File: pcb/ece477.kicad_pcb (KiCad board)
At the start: 2 copper layers, 44 x 40 mm, 16 parts, among them J1 USB_A, SW1 SW_DIP_x01, U1 ESP32-WROOM-32, U2 FT232RL-REEL, U3 LM3671, U4 ADA254, U5 ADA751

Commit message: squeezed lm3671 components together
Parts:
- moved L1 5.10 mm to (170.0, 86.0)
- moved C2 4.00 mm to (170.0, 84.0), turned to 270 degrees
- moved U3 4.00 mm to (173.0, 85.0)
- moved C3 0.34 mm to (174.3, 87.0), turned to 180 degrees
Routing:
- net Net-(C3-Pad2): track 21.0 -> 9.60 mm, vias 2 -> 0
- net Net-(C2-Pad2): track 99.5 -> 90.6 mm
- net Net-(L1-Pad2): track 3.29 -> 1.84 mm
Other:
- board text added: "1"

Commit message: pcb update
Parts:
- removed J1: USB_A, digikey-footprints:USB_Mini_B_Female_690-005-299-043
- removed U1: ESP32-WROOM-32, digikey-footprints:ESP32-WROOM-32D
- removed U4: ADA254, Connector_PinSocket_2.00mm:PinSocket_1x08_P2.00mm_Vertical
- added ADA 254: ADA254, Connector_PinSocket_2.00mm:PinSocket_1x08_P2.00mm_Vertical, F.Cu at (154.0, 111.0)
- added ESP32: ESP32-WROOM-32, digikey-footprints:ESP32-WROOM-32D, F.Cu at (159.0, 98.0)
- added MicroUSB: USB_B, Connector_USB:USB_Micro-B_Molex_47346-0001, F.Cu at (179.0, 95.0)
- ADA 751: renamed from U5
- renumbered U2 to FT232RL
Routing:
- net Net-(C2-Pad2): track 90.6 -> 95.8 mm
- net Net-(C3-Pad2): track 9.60 -> 14.5 mm
- net Net-(C5-Pad1): track 16.7 -> 19.2 mm
- net Net-(J1-Pad3): track 26.6 -> 28.9 mm
- net Net-(R1-Pad2): track 37.4 -> 35.0 mm
- net Net-(J1-Pad2): track 28.4 -> 30.8 mm

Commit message: shifted LM3671 to top right
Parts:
- removed ADA 751: ADA751, Connector_PinHeader_2.00mm:PinHeader_1x05_P2.00mm_Vertical
- removed FB1: Ferrite_Bead, Ferrite_THT:LairdTech_28C0236-0JW-10
- removed FT232RL: FT232RL-REEL, digikey-footprints:SSOP-28_W5.30mm
- added C6: 10uF, Capacitor_SMD:CP_Elec_3x5.3, F.Cu at (173.0, 86.5)
- added D1: LED, LED_SMD:LED_0201_0603Metric, F.Cu at (172.0, 95.0)
- added D2: LED, LED_SMD:LED_0201_0603Metric, F.Cu at (172.0, 97.5)
- added R2: 100kΩ, Resistor_SMD:R_0201_0603Metric, F.Cu at (181.5, 79.5)
- added R3: 1kΩ, Resistor_SMD:R_0201_0603Metric, F.Cu at (174.0, 95.0)
- added R4: 1kΩ, Resistor_SMD:R_0201_0603Metric, F.Cu at (174.0, 97.5)
- added U2: FT232RL-REEL, digikey-footprints:SSOP-28_W5.30mm, F.Cu at (177.0, 108.0)
- added U5: ADA751, Connector_PinHeader_2.00mm:PinHeader_1x05_P2.00mm_Vertical, F.Cu at (165.0, 78.5)
- C4: value 100nF -> 0.1uF
- C5: value 10nF -> 0.1uF
- U4: renamed from ADA 254
- moved C4 25.9 mm to (178.5, 102.0), turned to 0 degrees
- moved SW1 17.9 mm to (161.0, 84.5)
- moved C2 7.78 mm to (175.5, 78.5)
- moved C3 7.78 mm to (179.8, 81.5)
- moved L1 7.78 mm to (175.5, 80.5)
- moved U3 7.78 mm to (178.5, 79.5)
- moved C5 4.03 mm to (174.0, 92.5)
- moved R1 1.80 mm to (150.5, 111.0), turned to 0 degrees
- moved C1 1.01 mm to (178.5, 86.0), turned to 90 degrees
- moved BT1 1.00 mm to (182.0, 85.0)
- renumbered MicroUSB to J1, ESP32 to U1
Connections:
- U3 pad 3: Net-(C3-Pad2) -> Net-(R2-Pad1)
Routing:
- net Net-(U1-Pad35): track 4.80 -> 43.6 mm
- net Net-(U1-Pad34): track 12.4 -> 40.1 mm, vias 0 -> 2
- net Net-(J1-Pad2): track 30.8 -> 10.6 mm
- net Net-(C3-Pad2): track 14.5 -> 30.7 mm
- net Net-(J1-Pad3): track 28.9 -> 13.5 mm
- net Net-(BT1-Pad1): track 10.2 -> 20.1 mm
- net Net-(C4-Pad2): track 9.82 -> 2.99 mm
- net Net-(C2-Pad2): track 95.8 -> 102.4 mm, vias 2 -> 0
- net Net-(R1-Pad2): track 35.0 -> 30.9 mm
- net Net-(U1-Pad27): track 14.7 -> 17.4 mm
- net Net-(R2-Pad1): track 0.00 -> 2.09 mm
- net Net-(U1-Pad28): track 15.0 -> 17.1 mm
- net Net-(D2-Pad2): track 0.00 -> 2.00 mm
- net Net-(D1-Pad2): track 0.00 -> 2.00 mm
- net Net-(C5-Pad1): track 19.2 -> 20.2 mm
- added copper zone on B.Cu, net GND
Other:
- net class Power added: clearance 0.25, trace_width 0.5, via_dia 0.8, via_drill 0.4

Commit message: cleanup
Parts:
- moved C3 2.23 mm to (181.5, 80.0), turned to 270 degrees
- moved R2 1.50 mm to (181.5, 78.0), turned to 0 degrees
- turned C2 to 0 degrees
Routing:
- net Net-(C2-Pad2): track 102.4 -> 95.5 mm
- net Net-(C3-Pad2): track 30.7 -> 32.9 mm

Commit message: some fixes not done yet
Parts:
- C1, C2, C3, C4, C5: footprint Capacitor_SMD:C_0201_0603Metric -> Capacitor_SMD:C_0805_2012Metric
- C6: footprint Capacitor_SMD:CP_Elec_3x5.3 -> Capacitor_SMD:C_0805_2012Metric
- D1, D2: footprint LED_SMD:LED_0201_0603Metric -> LED_SMD:LED_0805_2012Metric
- L1: footprint Inductor_SMD:L_0201_0603Metric -> Inductor_SMD:L_0805_2012Metric
- R1, R2, R3, R4: footprint Resistor_SMD:R_0201_0603Metric -> Resistor_SMD:R_0805_2012Metric
- moved C3 56.1 mm to (129.7, 101.4), turned to 0 degrees
- moved R2 49.0 mm to (138.5, 101.4)
- moved C2 45.1 mm to (133.0, 93.5)
- moved L1 41.2 mm to (138.5, 98.5), turned to 0 degrees
- moved C5 7.52 mm to (174.5, 85.0), turned to 0 degrees
- moved D1 6.73 mm to (176.5, 100.0), turned to 270 degrees
- moved U3 6.02 mm to (172.5, 80.0)
- moved U5 6.00 mm to (159.0, 78.5)
- moved SW1 5.50 mm to (155.5, 84.5)
- moved R3 5.10 mm to (173.0, 100.0), turned to 270 degrees
- moved D2 4.92 mm to (176.5, 95.5)
- moved R4 2.24 mm to (173.0, 95.5)
- moved J1 2.00 mm to (181.0, 95.0)
- moved C6 1.80 mm to (174.5, 87.5)
- moved C4 1.00 mm to (179.5, 102.0)
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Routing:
- net Net-(C3-Pad2): track 32.9 -> 0.00 mm
- net Net-(U1-Pad27): track 17.4 -> 0.40 mm, vias 2 -> 0
- net Net-(U1-Pad28): track 17.1 -> 0.77 mm, vias 2 -> 0
- net Net-(D1-Pad1): track 0.00 -> 12.2 mm
- net Net-(D2-Pad1): track 0.00 -> 8.74 mm
- net Net-(C5-Pad1): track 20.2 -> 27.2 mm
- net Net-(BT1-Pad1): track 20.1 -> 14.4 mm
- net Net-(C2-Pad2): track 95.5 -> 92.3 mm
- net Net-(L1-Pad2): track 1.84 -> 0.00 mm
- net Net-(R2-Pad1): track 1.77 -> 0.00 mm
- net Net-(D2-Pad2): track 2.00 -> 3.50 mm
- net Net-(D1-Pad2): track 2.00 -> 3.50 mm
- net Net-(J1-Pad3): track 13.5 -> 14.3 mm

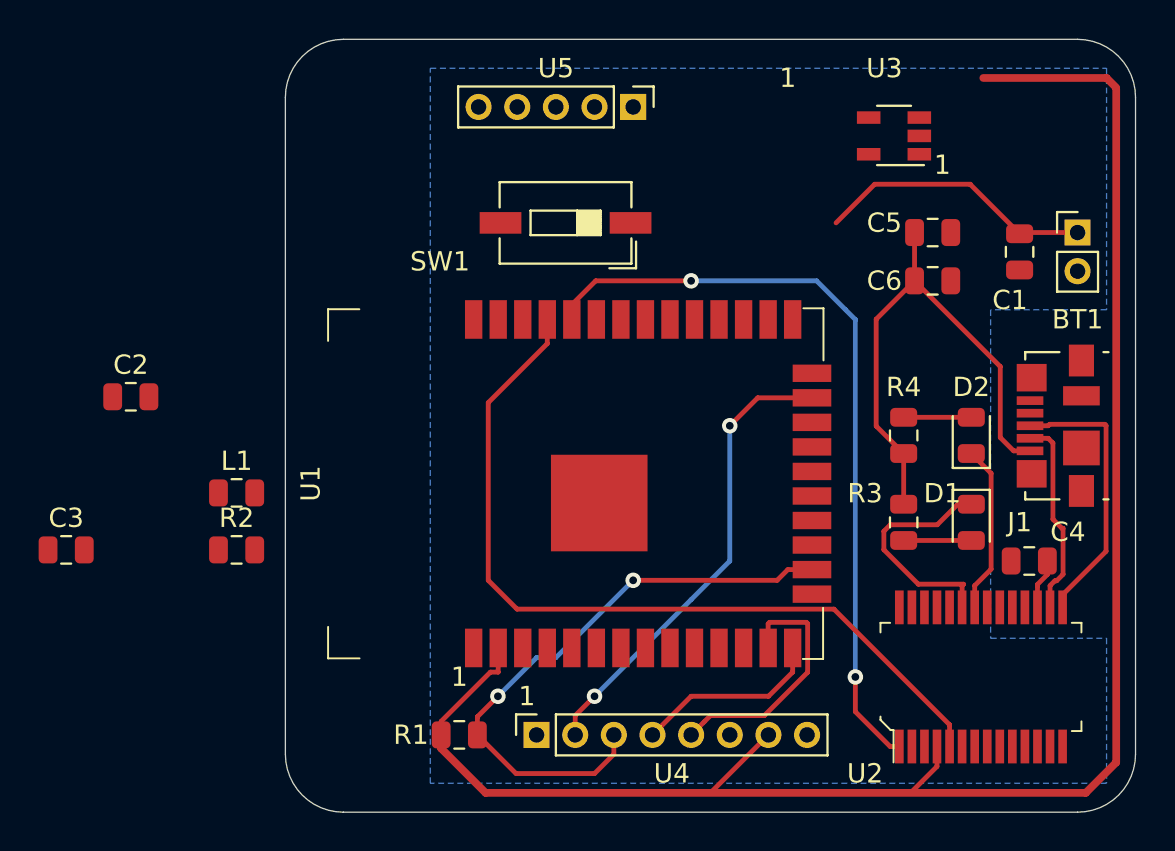
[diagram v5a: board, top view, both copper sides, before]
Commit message: updated C and R size, fixed LM3671
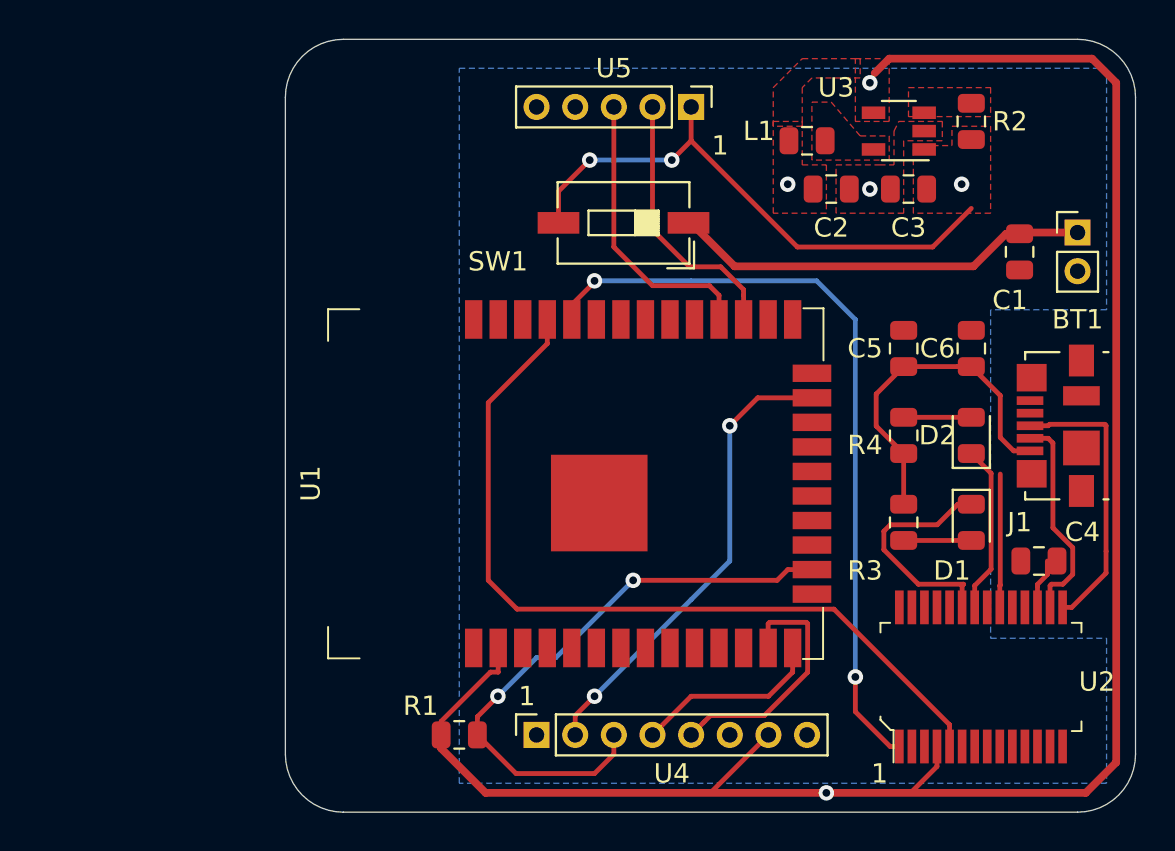
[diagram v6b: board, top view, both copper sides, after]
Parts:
- moved C3 47.4 mm to (173.2, 82.8)
- moved R2 44.0 mm to (176.5, 79.2), turned to 270 degrees
- moved C2 37.8 mm to (169.2, 82.8), turned to 180 degrees
- moved L1 34.7 mm to (168.0, 80.2)
- moved C5 6.18 mm to (173.0, 91.0), turned to 90 degrees
- moved C6 4.03 mm to (176.5, 91.0), turned to 90 degrees
- moved SW1 3.00 mm to (158.5, 84.5)
- moved U5 3.00 mm to (162.0, 78.5)
- moved C4 0.50 mm to (180.0, 102.0)
- moved U3 0.35 mm to (172.8, 79.8)
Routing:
- net Net-(C3-Pad2): track 0.00 -> 28.9 mm, vias 0 -> 3
- net Net-(U1-Pad28): track 0.77 -> 15.7 mm
- net Net-(U1-Pad27): track 0.40 -> 14.3 mm
- net Net-(BT1-Pad1): track 14.4 -> 21.7 mm
- net Net-(C2-Pad2): track 92.3 -> 98.9 mm, vias 0 -> 3
- net Net-(C5-Pad1): track 27.2 -> 24.8 mm
- net Net-(J1-Pad3): track 14.3 -> 15.3 mm
- net Net-(J1-Pad2): track 10.4 -> 11.0 mm
- net GND: vias 0 -> 1
- added copper zone on F.Cu, net GND
- added copper zone on F.Cu, net Net-(C2-Pad2)
- added copper zone on F.Cu, net Net-(C3-Pad2)
- added copper zone on F.Cu, net Net-(L1-Pad2)
- added copper zone on F.Cu, net Net-(R2-Pad1)
